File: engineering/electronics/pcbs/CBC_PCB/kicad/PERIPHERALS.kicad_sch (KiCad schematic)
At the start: 7 parts, among them J501 B08B-JWPF-SK-R

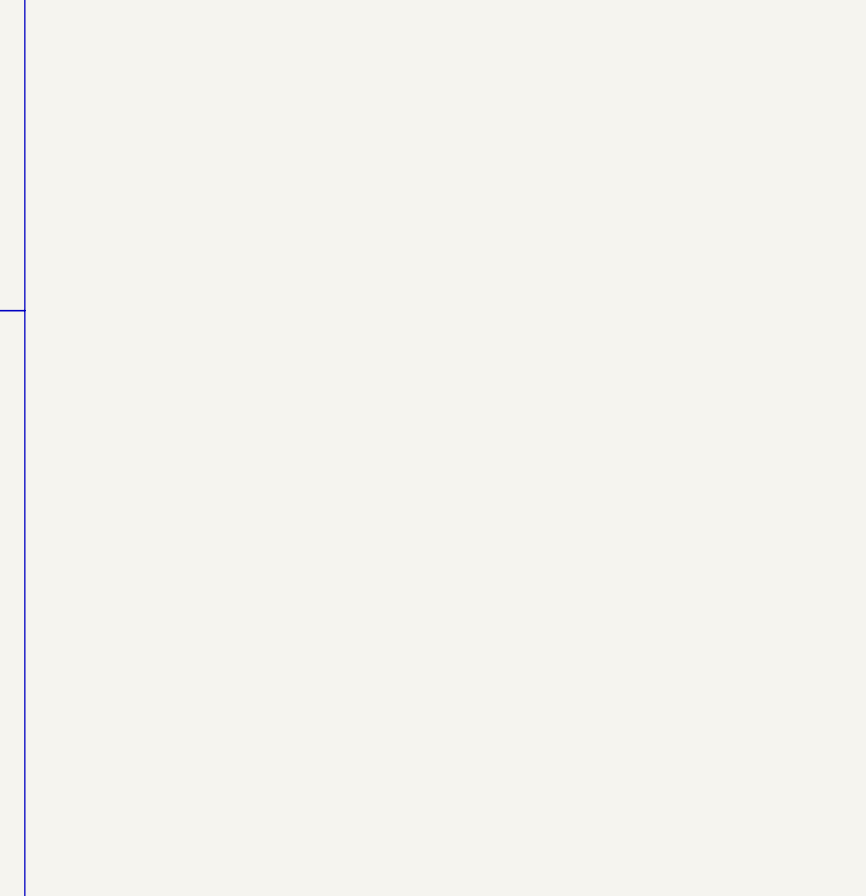
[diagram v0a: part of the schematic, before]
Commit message: feat(cbc): integrate PT1.5 CBC PCB update for the US build
Julius's CPC_PCB_21_10_26_5 package (issue #58): precharge ground fix with the new H_PWR-OUT- net and NT201, precharge and HV bus sensing, BZ501 buzzer, aux input inrush limiting (RT601, R628/R629, F604), BOM-review part swaps, and JLC production outputs. The board STEP is zipped because the raw export is 127 MB, which is over GitHub's 100 MB file limit.
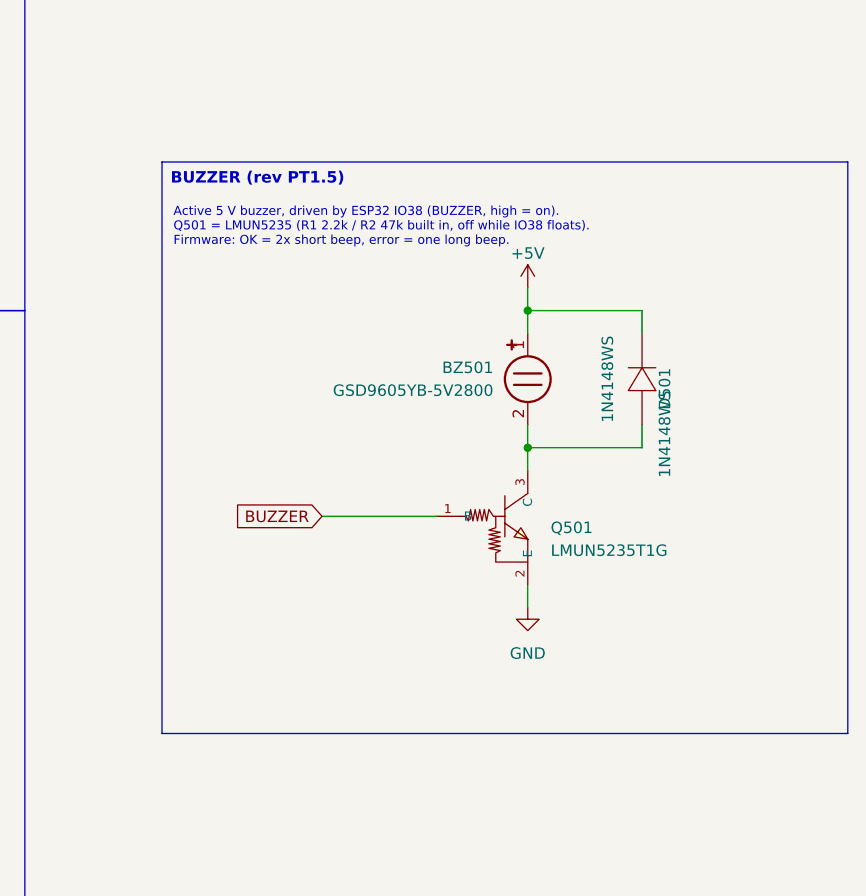
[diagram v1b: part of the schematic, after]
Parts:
- added BZ501: GSD9605YB-5V2800, CBC_PCB:BUZ-SMD_GSD9605YB-5V2800, symbol CBC_PCB:GSD9605YB-5V2800
- added D501: 1N4148WS, EasyEDA_Lib_2:SOD-323_L1.8-W1.3-LS2.5-RD, symbol EasyEDA_Lib_2:1N4148WS T4
- added Q501: LMUN5235T1G, lcsc_footprints:C2846922_SOT-323-3_L2_0-W1_3-P1_30-LS2_1-BR, symbol LCSC:LMUN5235T1G
- J501: Manufacturer (none) -> DLL; Manufacturer Part (none) -> DL20023-8AS; Supplier (none) -> LCSC; Supplier Part (none) -> C22374983
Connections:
- net GND: now also Q501.2 (E)
- new net: BZ501.2 (-), D501.2 (A), Q501.3 (C)
- new net +5V: BZ501.1 (+), D501.1 (K)
- new net BUZZER: Q501.1 (B)
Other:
- note added: "Active 5 V buzzer, driven by ESP32 IO38 (BUZZER, high = on). Q501 = LMUN5235 (R1 2.2k / R2 47k built in, off while IO38 floats). Firmware: OK = 2x short beep, error = one long beep."
